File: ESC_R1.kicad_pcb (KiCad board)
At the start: 2 copper layers, 174 parts, among them J101 Conn_01x03_Pin, J102 Conn_01x02_Pin, J103 Conn_01x02_Pin, J104 Conn_01x02_Pin, J201 Conn_01x05_Pin, J202 SWD TagConnect, J301 Conn_01x04_Male, J401 USB_C_Receptacle, Q501 BSC072N08NS5, Q502 BSC072N08NS5, Q601 BSC072N08NS5, Q602 BSC072N08NS5, Q701 BSC072N08NS5, Q702 BSC072N08NS5, SW201 PTS810 SJK, U101 TPS54332D, U102 TPS561208D, U103 TLV75533PDBV, U201 STM32F446RETx, U301 TJA1441AT, U401 USBLC6-2SC6, U501 IR2181S, U502 AD8418, U601 IR2181S, U602 AD8418, U701 IR2181S, U702 AD8418, Y201 16MHz

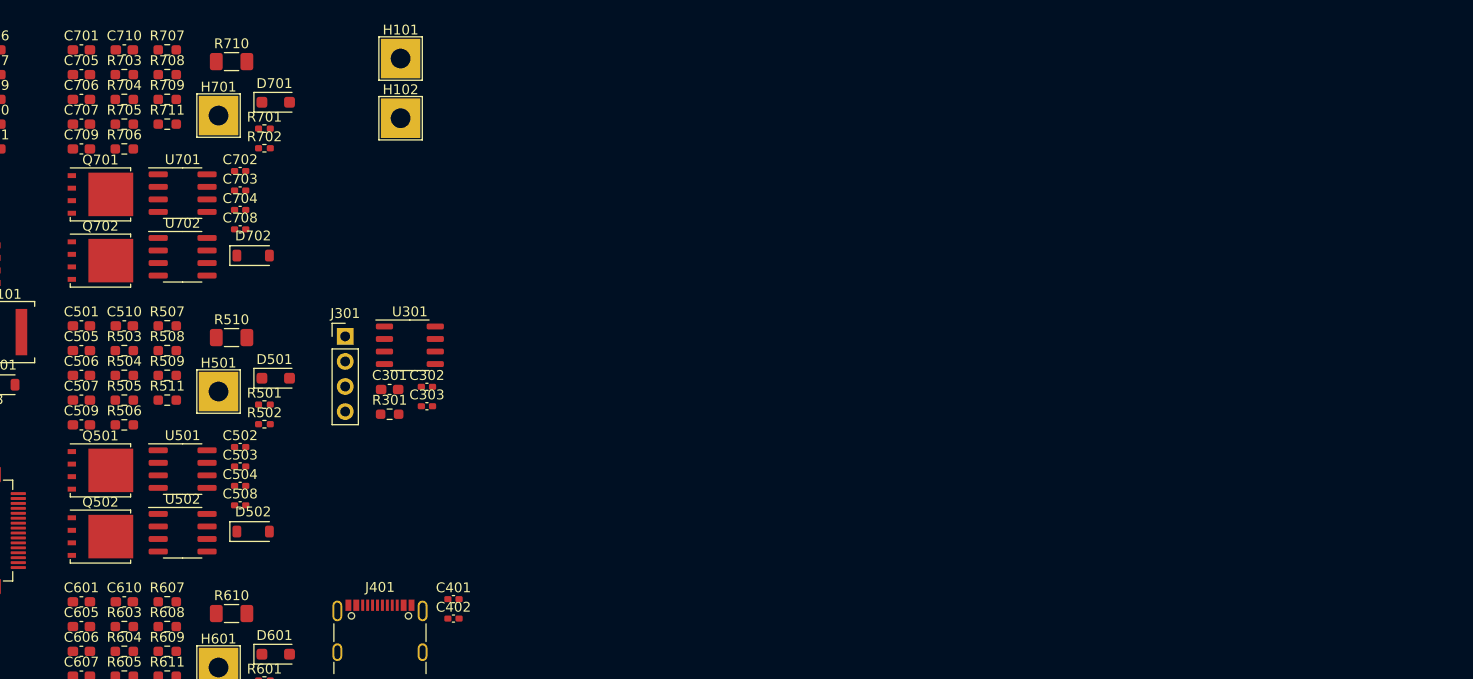
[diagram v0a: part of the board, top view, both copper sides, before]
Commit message: feat: initial layout of phase C
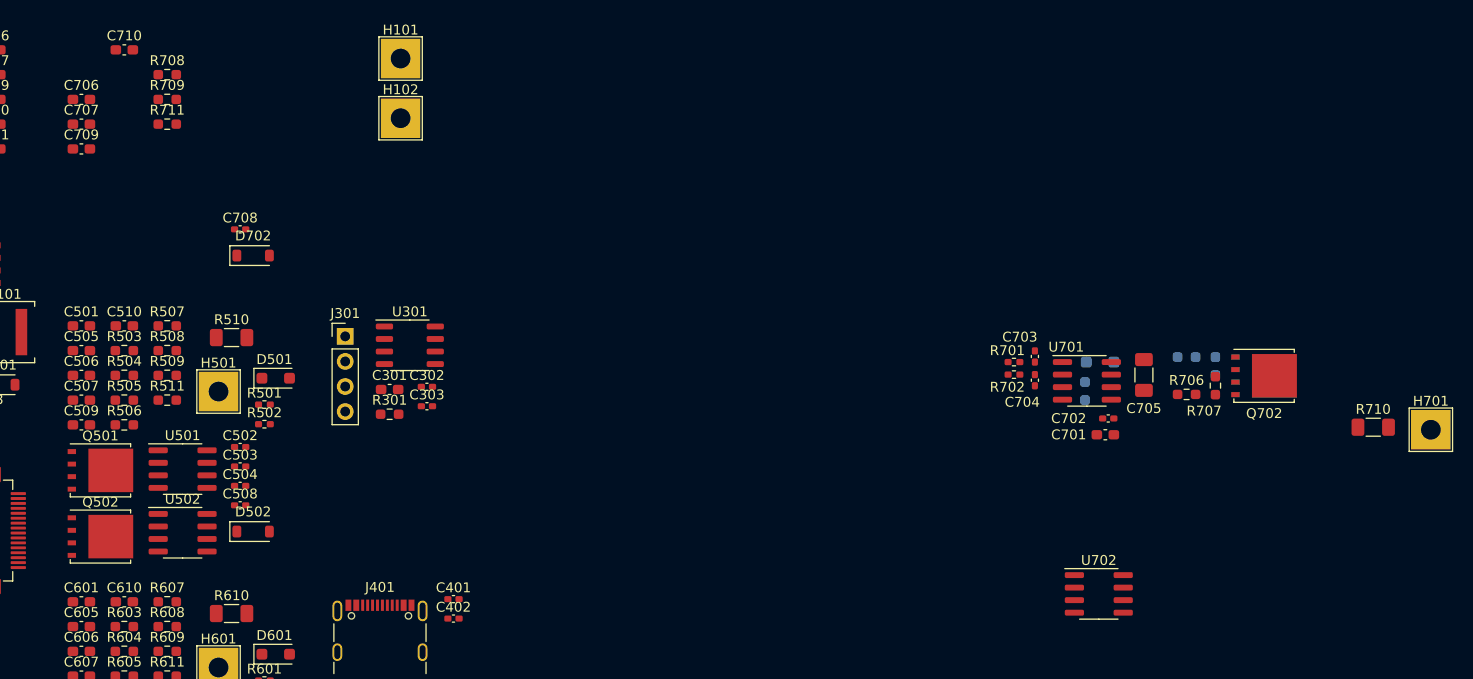
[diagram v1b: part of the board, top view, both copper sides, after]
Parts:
- C705: footprint Capacitor_SMD:C_0603_1608Metric_Pad1.08x0.95mm_HandSolder -> Capacitor_SMD:C_1206_3216Metric_Pad1.33x1.80mm_HandSolder
- D701, Q701, R703, R704, R705: moved to B.Cu
- moved H701 126.9 mm to (186.1, 56.4)
- moved R710 121.5 mm to (180.2, 56.1)
- moved Q701 119.4 mm to (169.1, 50.9)
- moved Q702 118.5 mm to (169.1, 50.9)
- moved R705 113.3 mm to (164.2, 49.9), turned to 90 degrees
- moved C705 111.9 mm to (157.0, 50.8), turned to -90 degrees
- moved R707 111.6 mm to (164.2, 51.9), turned to -90 degrees
- moved C701 110.9 mm to (153.1, 56.9)
- moved R704 110.8 mm to (161.3, 49.0)
- moved R706 110.5 mm to (161.3, 52.8)
- moved R703 102.5 mm to (151.0, 52.5), turned to 90 degrees
- moved U702 98.9 mm to (152.4, 73.0)
- moved U701 93.6 mm to (151.2, 51.4)
- moved C702 91.5 mm to (153.4, 55.2)
- moved D701 87.6 mm to (152.5, 49.5), turned to 180 degrees
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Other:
- copper layers 2 -> 4

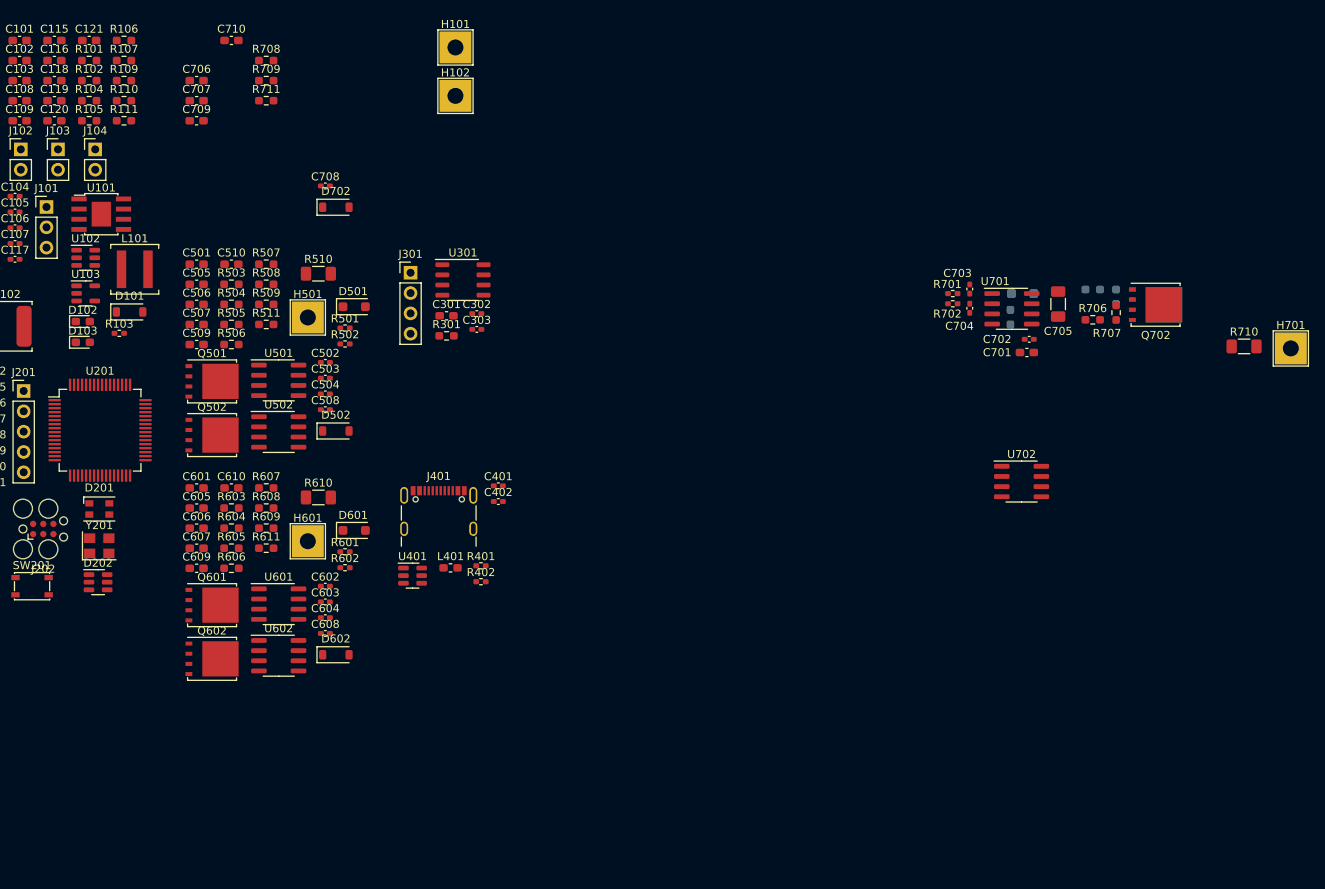
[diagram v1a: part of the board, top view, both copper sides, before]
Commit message: feat: component placement for 1 phase completed
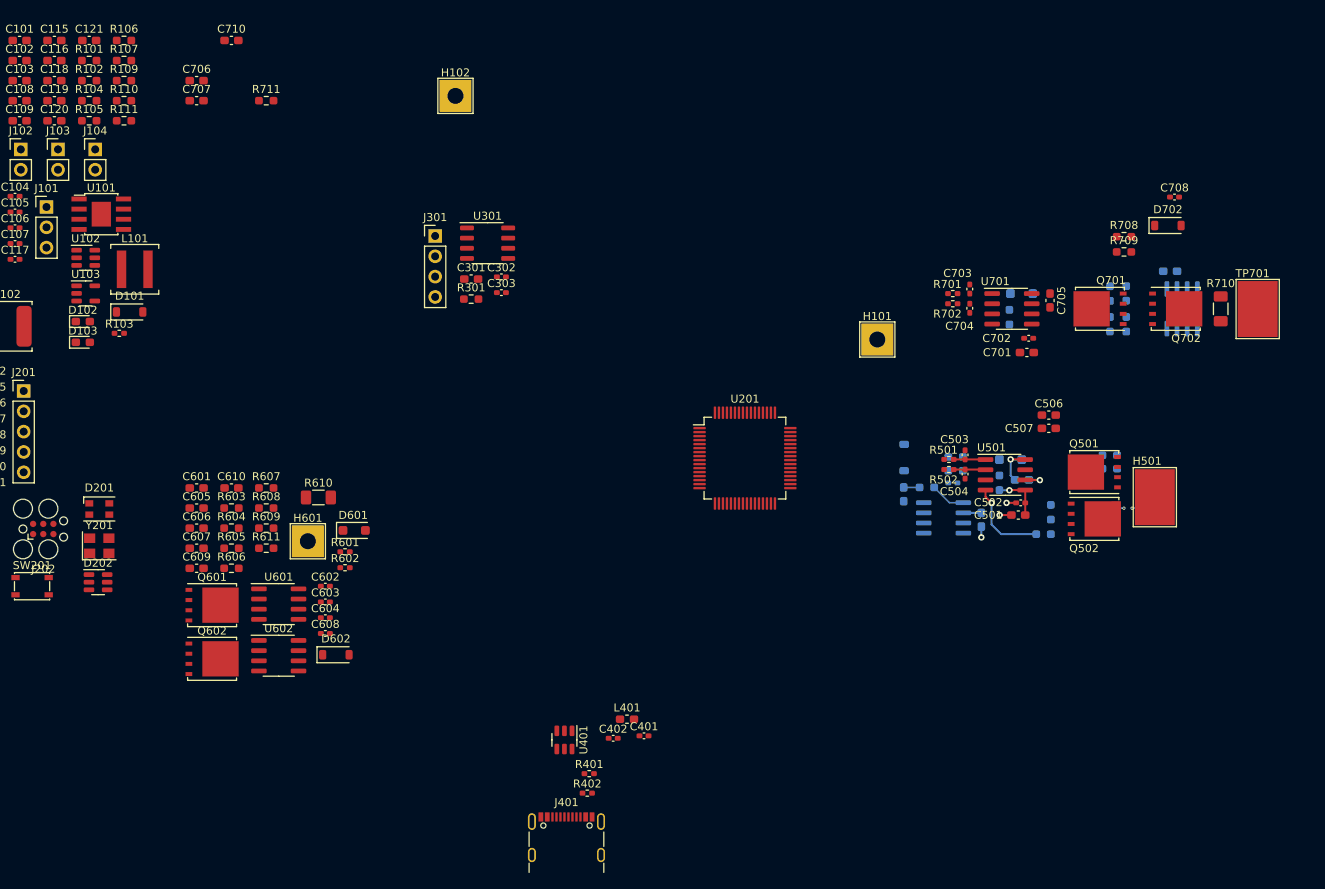
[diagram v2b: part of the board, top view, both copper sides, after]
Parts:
- removed H701: Pad, TestPoint:TestPoint_THTPad_4.0x4.0mm_Drill2.0mm
- added TP701: TestPoint, TestPoint:TestPoint_Pad_5.0x7.0mm, F.Cu at (181.9, 51.5)
- C505, C508, C509, C510, C709, D501, D502, R503, R504, R505, R506, R507, R508, R509, R510, R511, R706, R707, U502, U702: moved to B.Cu
- C705: footprint Capacitor_SMD:C_1206_3216Metric_Pad1.33x1.80mm_HandSolder -> Capacitor_SMD:C_0603_1608Metric_Pad1.08x0.95mm_HandSolder
- H501: footprint TestPoint:TestPoint_THTPad_4.0x4.0mm_Drill2.0mm -> TestPoint:TestPoint_Pad_5.0x7.0mm
- Q701: moved to F.Cu
- moved C709 123.1 mm to (171.0, 46.7)
- moved R504 111.4 mm to (163.4, 69.7)
- moved R505 111.3 mm to (163.4, 71.4), turned to 180 degrees
- moved Q501 110.9 mm to (161.5, 71.8), turned to 180 degrees
- moved Q502 110.8 mm to (161.5, 77.7)
- moved R708 109.5 mm to (165.2, 42.4)
- moved R709 109.3 mm to (165.2, 44.3)
- moved H501 108.2 mm to (169.1, 75.0)
- moved C506 107.4 mm to (155.8, 64.7)
- moved C501 107.4 mm to (152.0, 77.2)
- moved C507 107.3 mm to (155.8, 66.4)
- moved C708 106.2 mm to (171.5, 37.5)
- moved C505 106.0 mm to (152.4, 72.8)
- moved R510 105.4 mm to (165.7, 76.4)
- moved R506 104.2 mm to (155.1, 79.6)
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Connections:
- net /3-Phase Bridge - Phase A/PHA_PAD renamed /3-Phase Bridge - Phase A/PHA_CIN-
- net /3-Phase Bridge - Phase A/PHA_VS renamed /3-Phase Bridge - Phase A/PHA_CIN+
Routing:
- net /3-Phase Bridge - Phase A/PHA_LOUT: track 0.00 -> 10.7 mm, vias 0 -> 1
- net +12V: track 0.00 -> 6.37 mm, vias 0 -> 1
- net /3-Phase Bridge - Phase A/PHA_VB: track 0.00 -> 6.03 mm, vias 0 -> 1
- net PHA_C: track 0.00 -> 4.43 mm
- net /3-Phase Bridge - Phase A/PHA_CIN+: track 0.00 -> 4.28 mm, vias 0 -> 2
- net GND: track 0.00 -> 4.23 mm, vias 0 -> 3
- net /3-Phase Bridge - Phase A/PHA_IR_LIN: track 0.00 -> 3.99 mm
- net /3-Phase Bridge - Phase A/PHA_IR_HIN: track 0.00 -> 3.99 mm
- net +3.3V: track 0.00 -> 2.25 mm
- net PHA_CF: track 0.00 -> 1.98 mm
- net /3-Phase Bridge - Phase A/PHA_CIN-: track 0.00 -> 1.04 mm, vias 0 -> 1

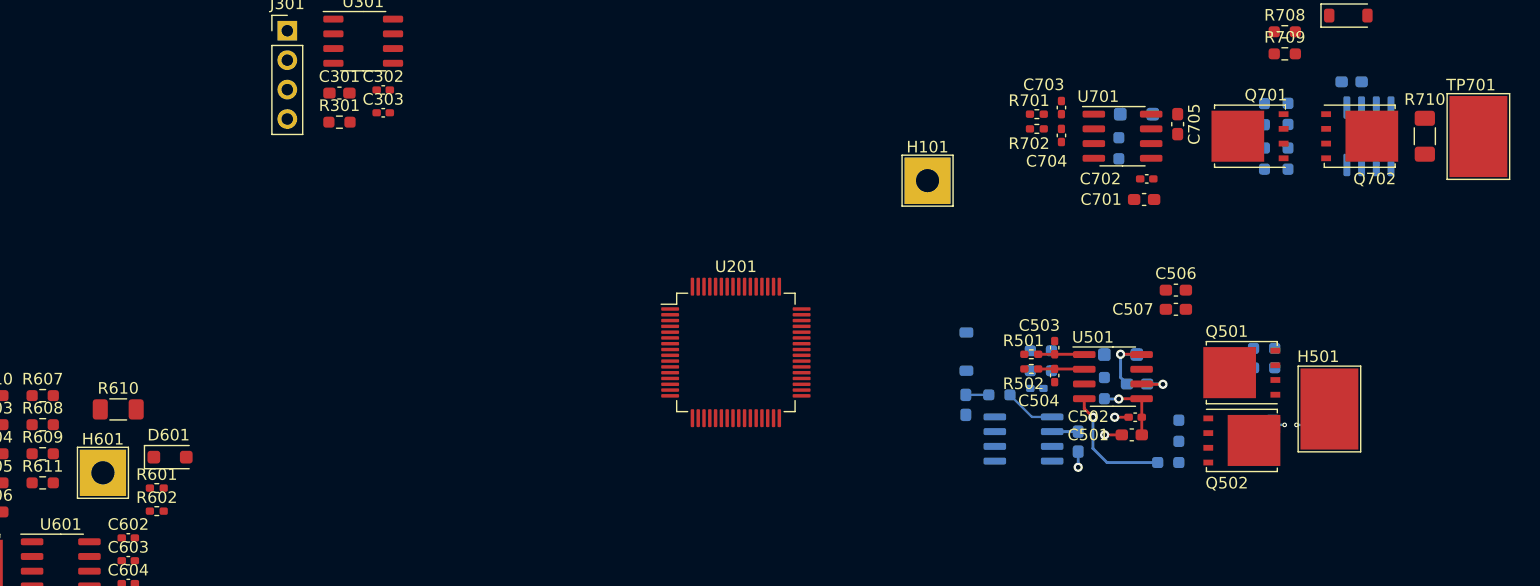
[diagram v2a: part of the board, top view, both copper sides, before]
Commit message: fix: fixed LTSpice simulation and updated track widths accordingly
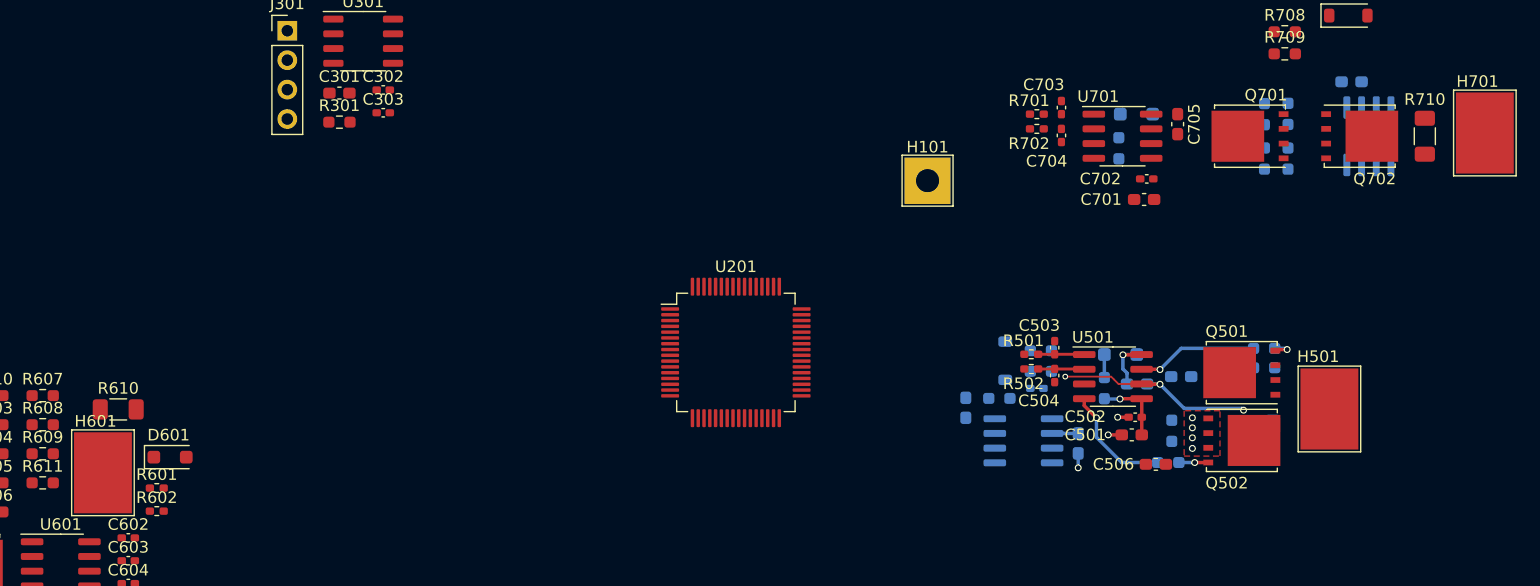
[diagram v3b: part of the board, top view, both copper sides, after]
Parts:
- removed TP701: TestPoint, TestPoint:TestPoint_Pad_5.0x7.0mm
- added H701: Pad, TestPoint:TestPoint_Pad_5.0x7.0mm, F.Cu at (182.5, 51.2)
- C507: moved to B.Cu
- H601: footprint TestPoint:TestPoint_THTPad_4.0x4.0mm_Drill2.0mm -> TestPoint:TestPoint_Pad_5.0x7.0mm
- moved C506 15.1 mm to (154.1, 79.8)
- moved C507 5.83 mm to (156.3, 72.2)
- moved D502 3.44 mm to (141.1, 70.8)
- moved R507 0.61 mm to (155.4, 76.9)
- moved R511 0.30 mm to (140.6, 74.1)
- moved C510 0.25 mm to (137.7, 74.9)
- moved C509 0.15 mm to (147.4, 78.0)
- moved U502 0.15 mm to (142.6, 77.7)
- moved R508 0.05 mm to (144.2, 71.7)
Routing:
- net /3-Phase Bridge - Phase A/PHA_CIN+: track 4.28 -> 17.7 mm, vias 2 -> 3
- net /3-Phase Bridge - Phase A/PHA_HOUT: track 0.00 -> 10.4 mm, vias 0 -> 1
- net PHA_C: track 4.43 -> 0.00 mm
- net /3-Phase Bridge - Phase A/PHA_LOUT_G: track 0.00 -> 2.54 mm, vias 0 -> 1
- net /3-Phase Bridge - Phase A/PHA_HOUT_G: track 0.00 -> 2.17 mm, vias 0 -> 1
- net /3-Phase Bridge - Phase A/PHA_VRD: track 0.00 -> 1.98 mm
- net PHA_CF: track 1.98 -> 0.00 mm
- net /3-Phase Bridge - Phase A/PHA_CIN-: track 1.04 -> 0.00 mm, vias 1 -> 0
- net /3-Phase Bridge - Phase A/PHA_LOUT: track 10.7 -> 9.95 mm
- net GND: track 4.23 -> 3.57 mm
- net /3-Phase Bridge - Phase A/PHA_VB: track 6.03 -> 5.49 mm
- net (no net): vias 0 -> 4
- added copper zone on F.Cu, net GND
